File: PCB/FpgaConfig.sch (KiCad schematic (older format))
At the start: 16 parts, among them J5 TSM-105-01-S-DV, U2 10CL016YE144C8G, U3 S25FL128SAGMFI000, X1 X1G0044510011

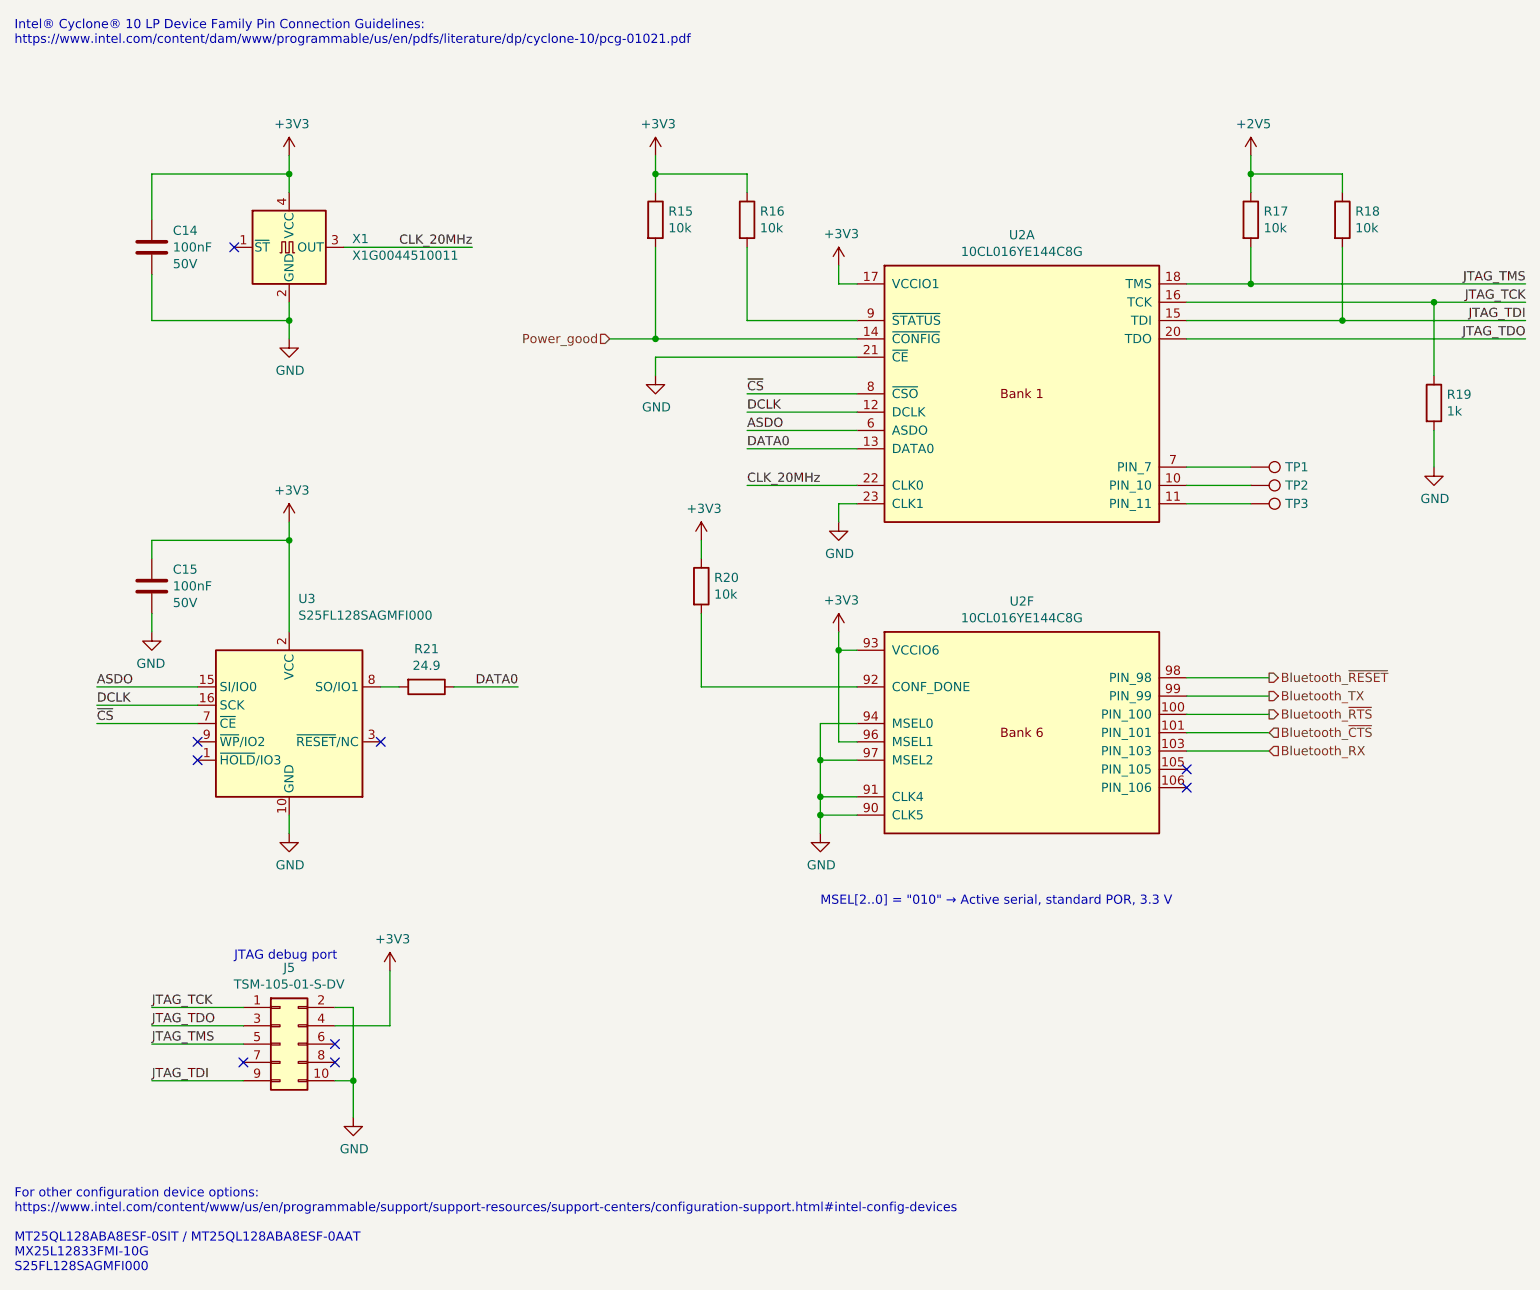
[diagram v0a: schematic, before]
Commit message: Add jumpers on the power supply outputs
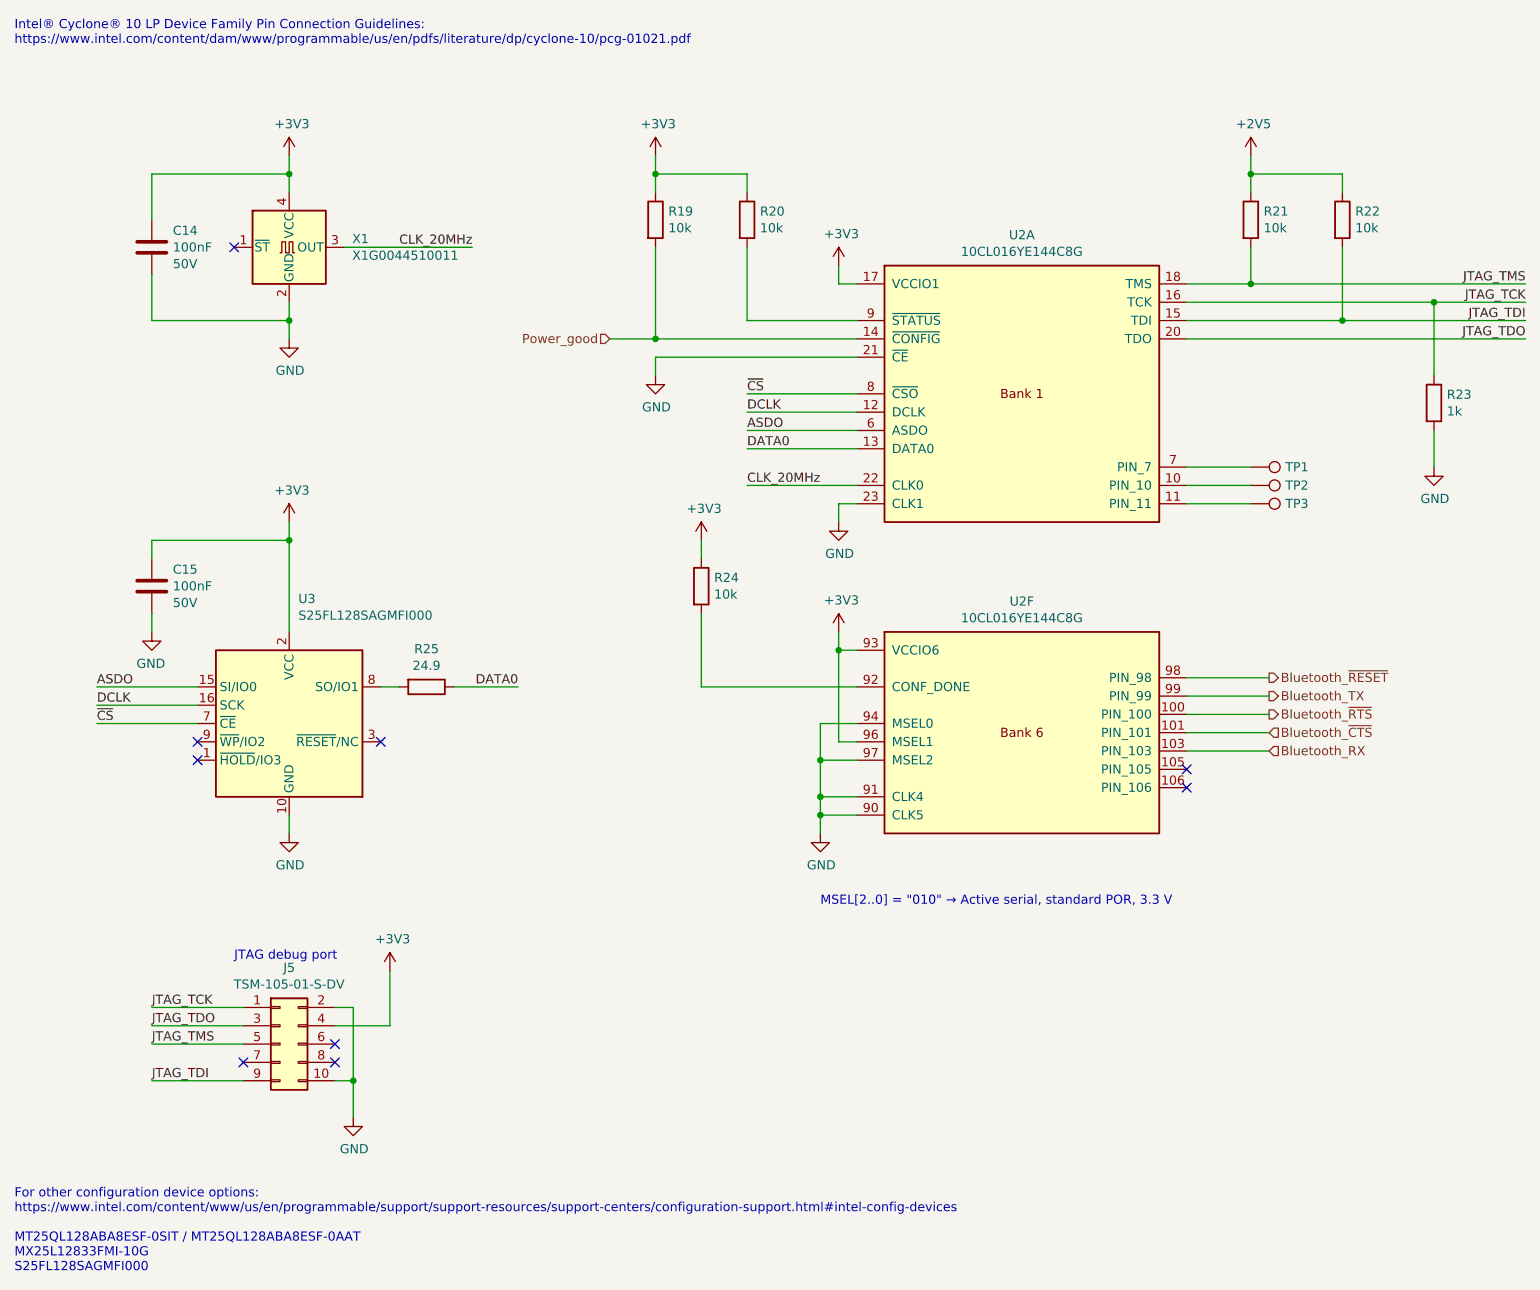
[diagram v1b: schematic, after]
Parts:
- renumbered R15 to R19, R16 to R20, R17 to R21, R18 to R22, R19 to R23, R20 to R24, R21 to R25
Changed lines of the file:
@@
 Sheet 4 23
 Title "Litter Robot 3 - FPGA configuration"
-Date "2021-04-10"
+Date "2021-05-24"
 Rev "A1"
 Comp "L. Sartory"
@@
 AR Path="/603F1DCE/6061CF64" Ref="R?"  Part="1"
 AR Path="/60624089/6061CF64" Ref="R?"  Part="1"
-AR Path="/603F1F4D/60647CC2/6061CF64" Ref="R16"  Part="1"
-F 0 "R16" H 4820 1796 50  0000 L CNN
+AR Path="/603F1F4D/60647CC2/6061CF64" Ref="R20"  Part="1"
+F 0 "R20" H 4820 1796 50  0000 L CNN
 F 1 "10k" H 4820 1705 50  0000 L CNN
 F 2 "Resistor_SMD:R_0603_1608Metric" V 4680 1750 50  0001 C CNN
@@
 AR Path="/603F1DCE/60629280" Ref="R?"  Part="1"
 AR Path="/60624089/60629280" Ref="R?"  Part="1"
-AR Path="/603F1F4D/60647CC2/60629280" Ref="R19"  Part="1"
-F 0 "R19" H 8570 2796 50  0000 L CNN
+AR Path="/603F1F4D/60647CC2/60629280" Ref="R23"  Part="1"
+F 0 "R23" H 8570 2796 50  0000 L CNN
 F 1 "1k" H 8570 2705 50  0000 L CNN
 F 2 "Resistor_SMD:R_0603_1608Metric" V 8430 2750 50  0001 C CNN
@@
 AR Path="/603F1DCE/60629C28" Ref="R?"  Part="1"
 AR Path="/60624089/60629C28" Ref="R?"  Part="1"
-AR Path="/603F1F4D/60647CC2/60629C28" Ref="R17"  Part="1"
-F 0 "R17" H 7570 1796 50  0000 L CNN
+AR Path="/603F1F4D/60647CC2/60629C28" Ref="R21"  Part="1"
+F 0 "R21" H 7570 1796 50  0000 L CNN
 F 1 "10k" H 7570 1705 50  0000 L CNN
 F 2 "Resistor_SMD:R_0603_1608Metric" V 7430 1750 50  0001 C CNN
@@
 AR Path="/603F1DCE/6062A70D" Ref="R?"  Part="1"
 AR Path="/60624089/6062A70D" Ref="R?"  Part="1"
-AR Path="/603F1F4D/60647CC2/6062A70D" Ref="R18"  Part="1"
-F 0 "R18" H 8070 1796 50  0000 L CNN
+AR Path="/603F1F4D/60647CC2/6062A70D" Ref="R22"  Part="1"
+F 0 "R22" H 8070 1796 50  0000 L CNN
 F 1 "10k" H 8070 1705 50  0000 L CNN
 F 2 "Resistor_SMD:R_0603_1608Metric" V 7930 1750 50  0001 C CNN
@@
 AR Path="/603F1DCE/606388B5" Ref="R?"  Part="1"
 AR Path="/60624089/606388B5" Ref="R?"  Part="1"
-AR Path="/603F1F4D/60647CC2/606388B5" Ref="R20"  Part="1"
-F 0 "R20" H 4570 3796 50  0000 L CNN
+AR Path="/603F1F4D/60647CC2/606388B5" Ref="R24"  Part="1"
+F 0 "R24" H 4570 3796 50  0000 L CNN
 F 1 "10k" H 4570 3705 50  0000 L CNN
 F 2 "Resistor_SMD:R_0603_1608Metric" V 4430 3750 50  0001 C CNN
@@
 DATA0
 $Comp
-L Device:R R21
+L Device:R R25
 U 1 1 6066CAE2
 P 3000 4300
-F 0 "R21" V 2793 4300 50  0000 C CNN
+F 0 "R25" V 2793 4300 50  0000 C CNN
 F 1 "24.9" V 2884 4300 50  0000 C CNN
 F 2 "Resistor_SMD:R_0603_1608Metric" V 2930 4300 50  0001 C CNN
@@
 AR Path="/603F1DCE/6069D386" Ref="R?"  Part="1"
 AR Path="/60624089/6069D386" Ref="R?"  Part="1"
-AR Path="/603F1F4D/60647CC2/6069D386" Ref="R15"  Part="1"
-F 0 "R15" H 4320 1796 50  0000 L CNN
+AR Path="/603F1F4D/60647CC2/6069D386" Ref="R19"  Part="1"
+F 0 "R19" H 4320 1796 50  0000 L CNN
 F 1 "10k" H 4320 1705 50  0000 L CNN
 F 2 "Resistor_SMD:R_0603_1608Metric" V 4180 1750 50  0001 C CNN
